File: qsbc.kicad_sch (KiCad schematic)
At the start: 0 parts

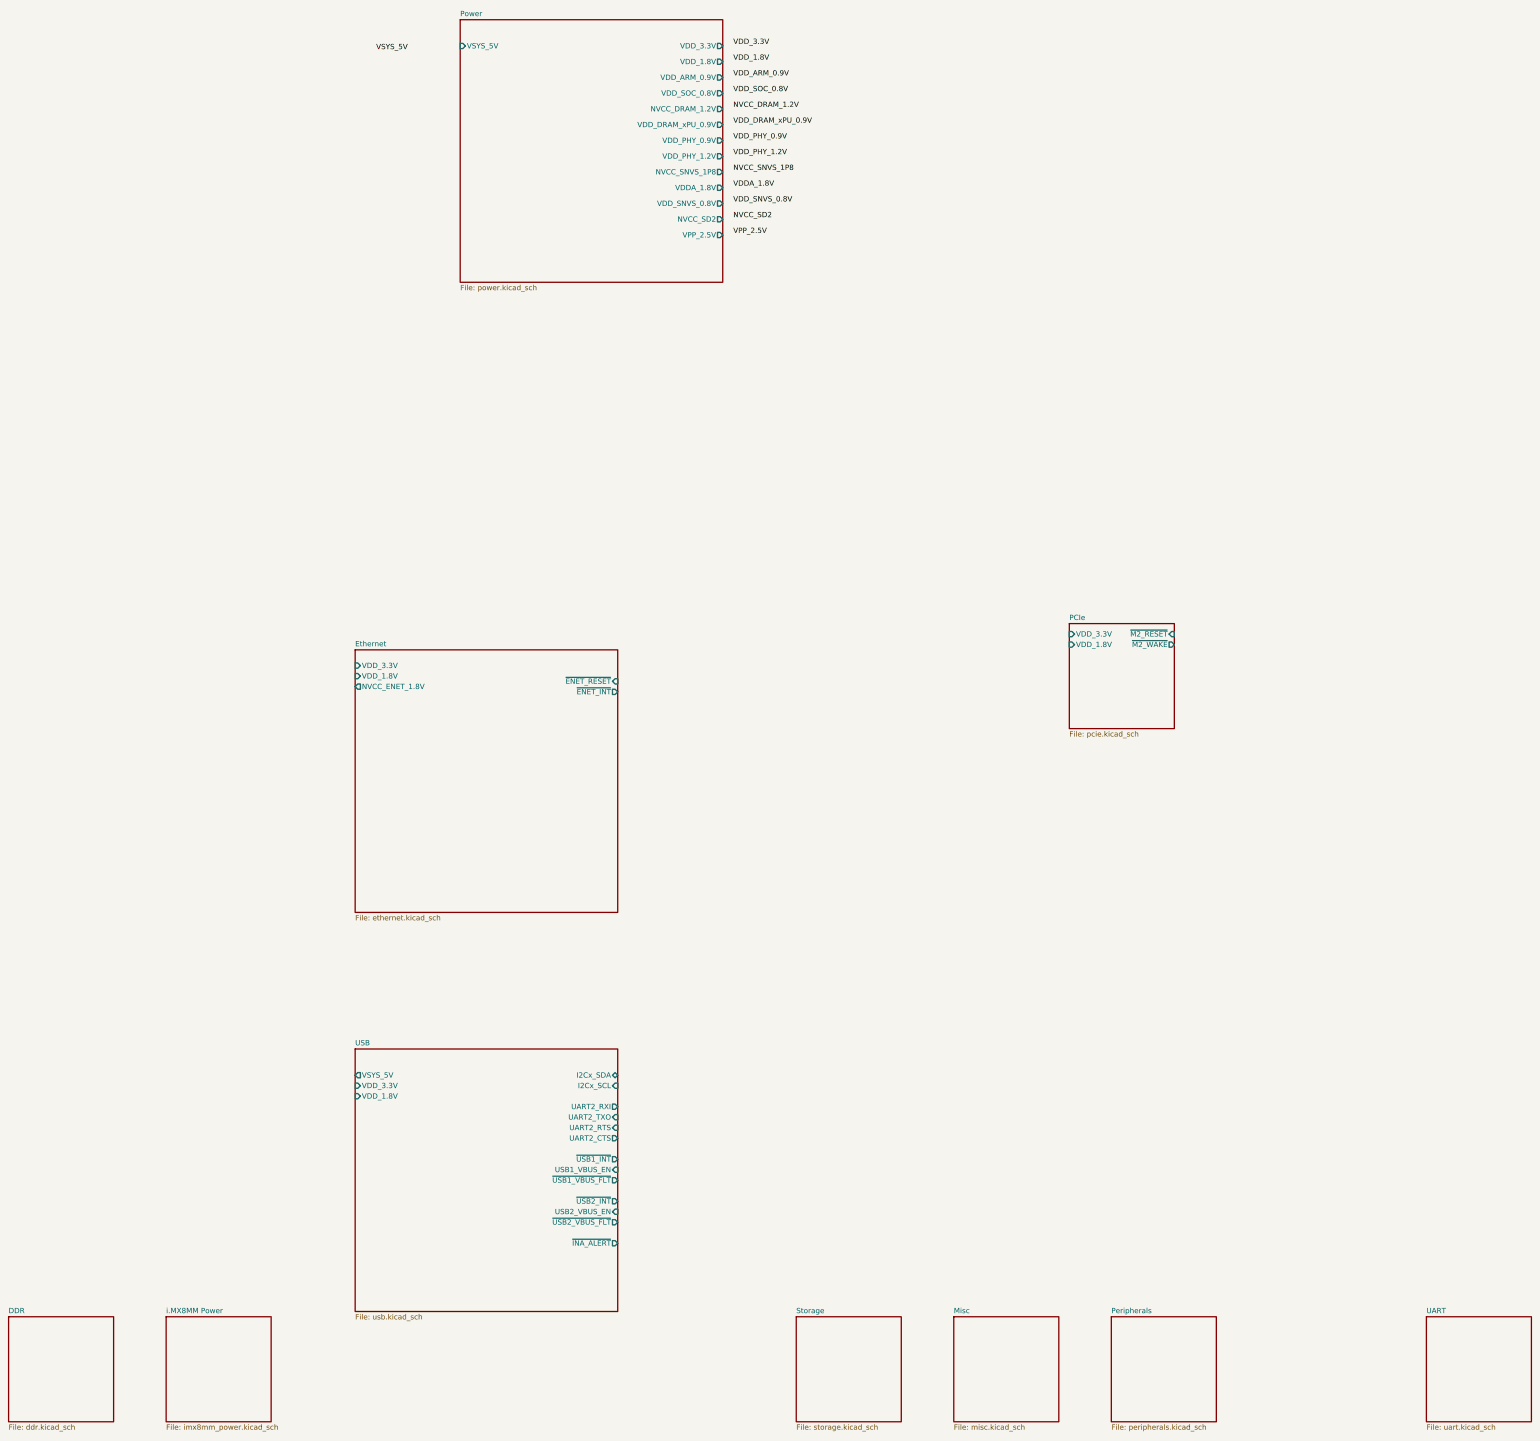
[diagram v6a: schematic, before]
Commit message: storage done, peri work, misc fixes
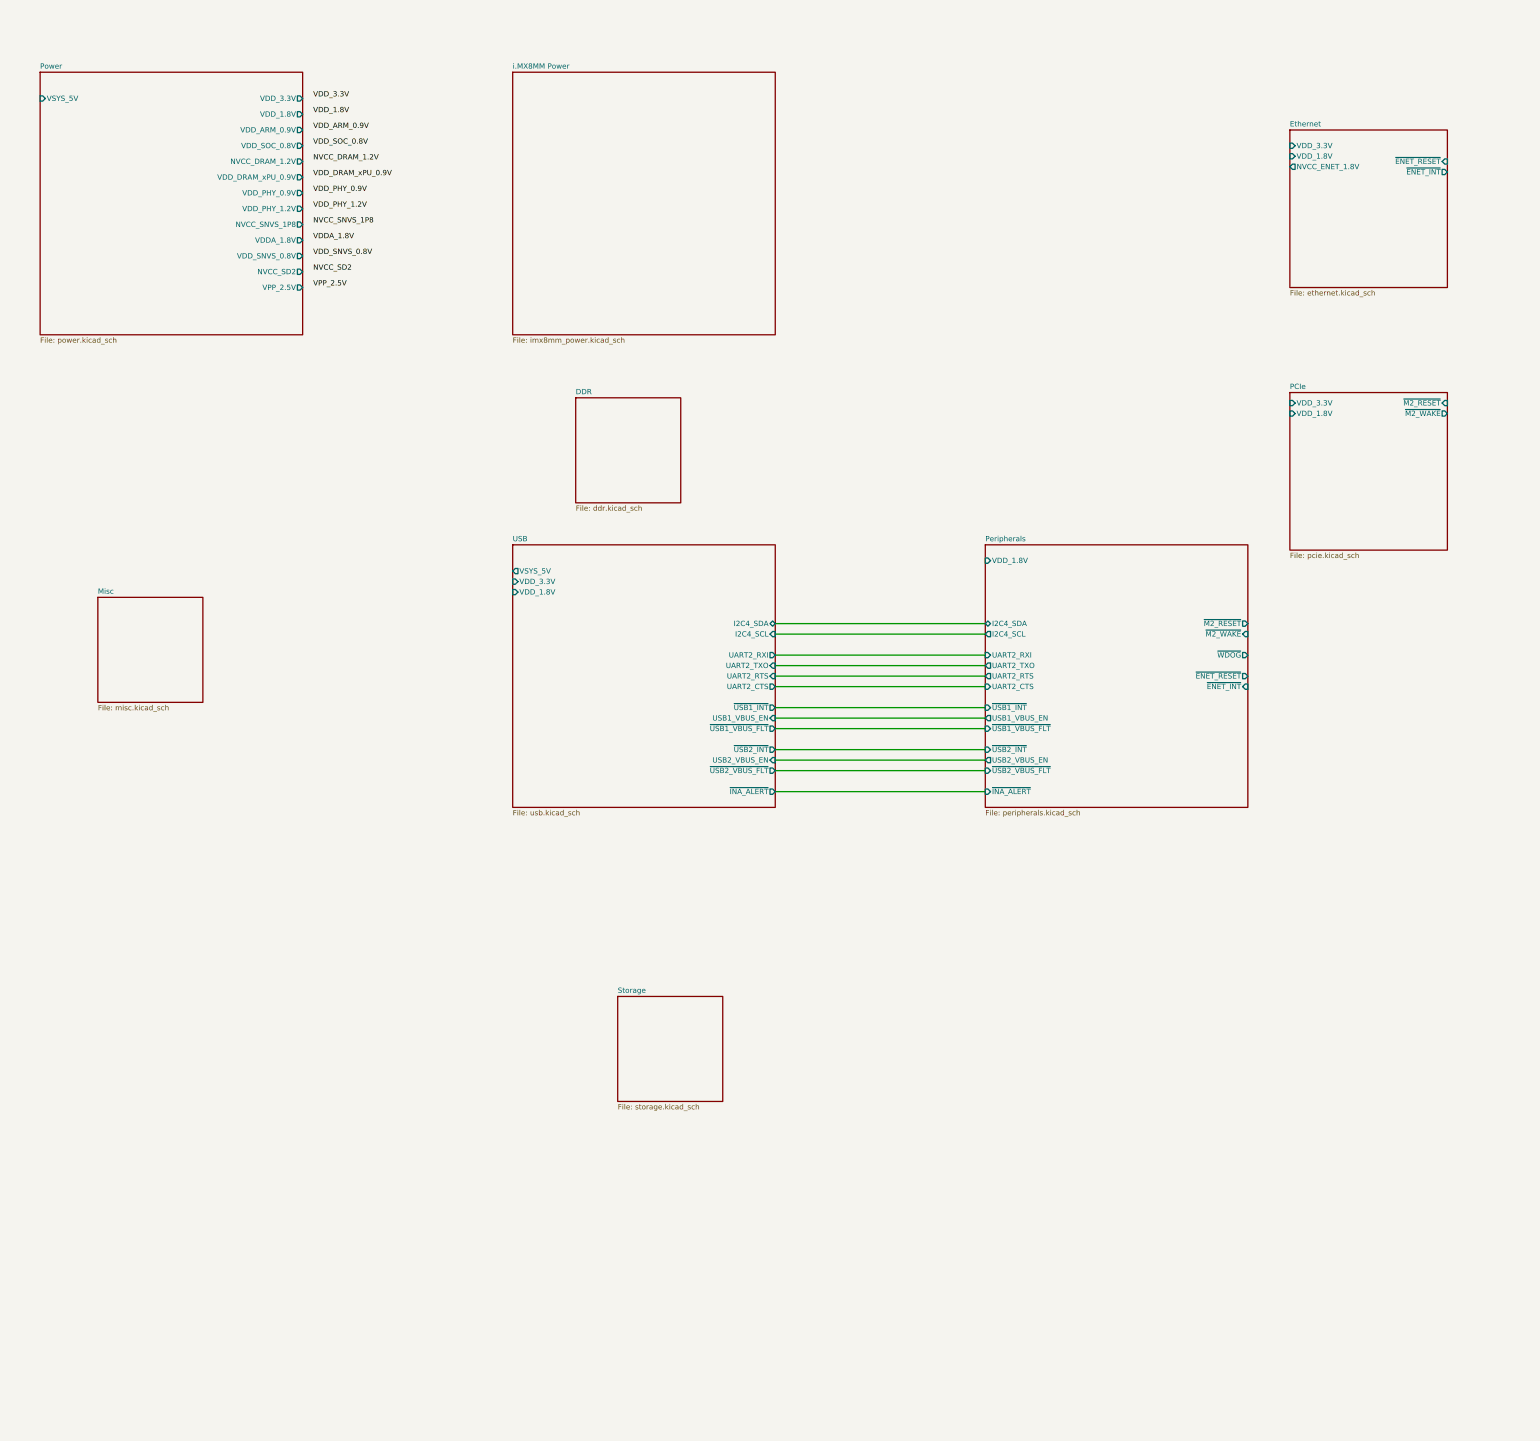
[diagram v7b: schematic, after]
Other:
- removed sheet UART
- sheet Peripherals ports: added I2C4_SCL, I2C4_SDA, UART2_CTS, UART2_RTS, UART2_RXI, UART2_TXO, USB1_VBUS_EN, USB2_VBUS_EN, VDD_1.8V, ~{ENET_INT}, ~{ENET_RESET}, ~{INA_ALERT}, ~{M2_RESET}, ~{M2_WAKE}, ~{USB1_INT}, ~{USB1_VBUS_FLT}, ~{USB2_INT}, ~{USB2_VBUS_FLT}, ~{WDOG}; removed none
- sheet USB ports: added I2C4_SCL, I2C4_SDA; removed I2Cx_SCL, I2Cx_SDA

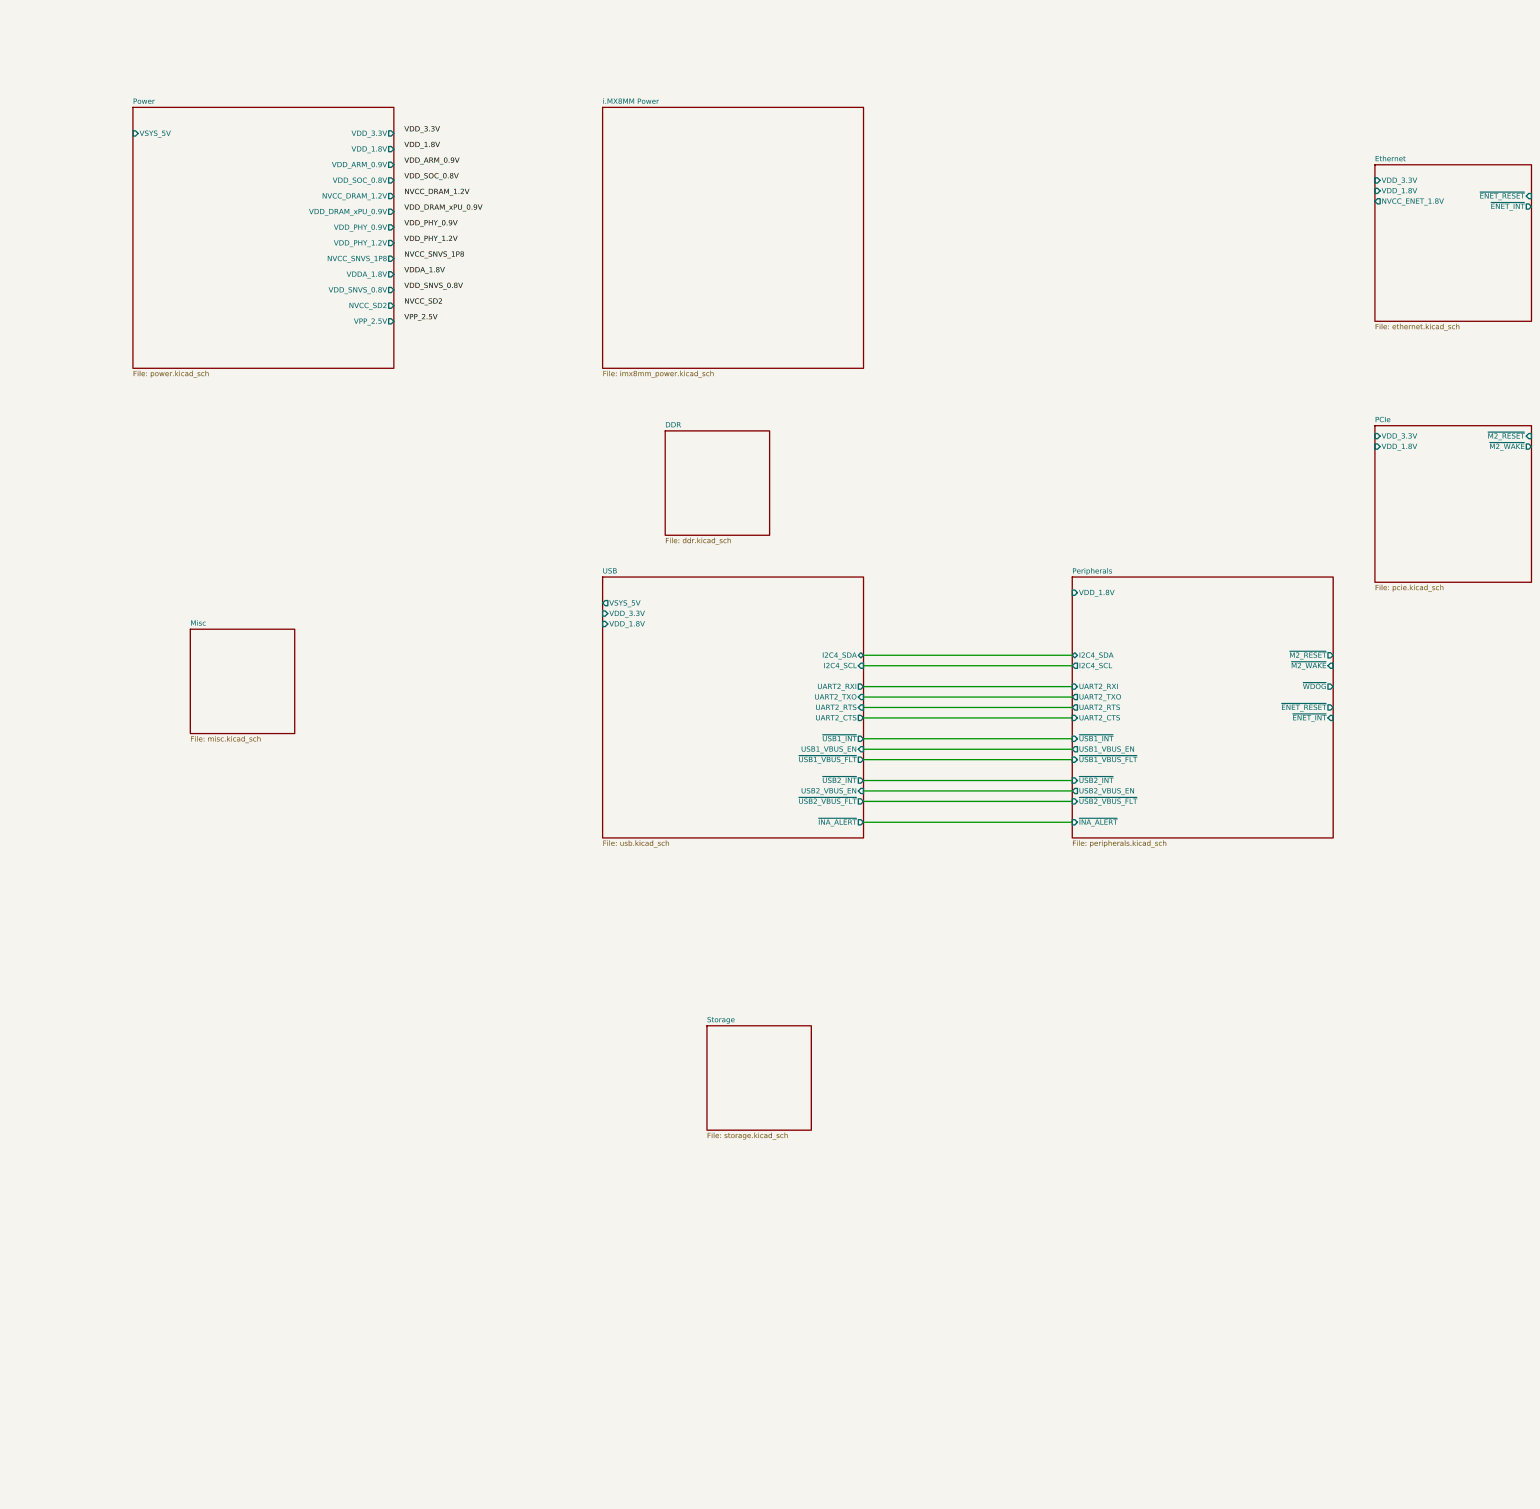
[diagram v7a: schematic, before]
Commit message: ddr: add dual die support, misc work
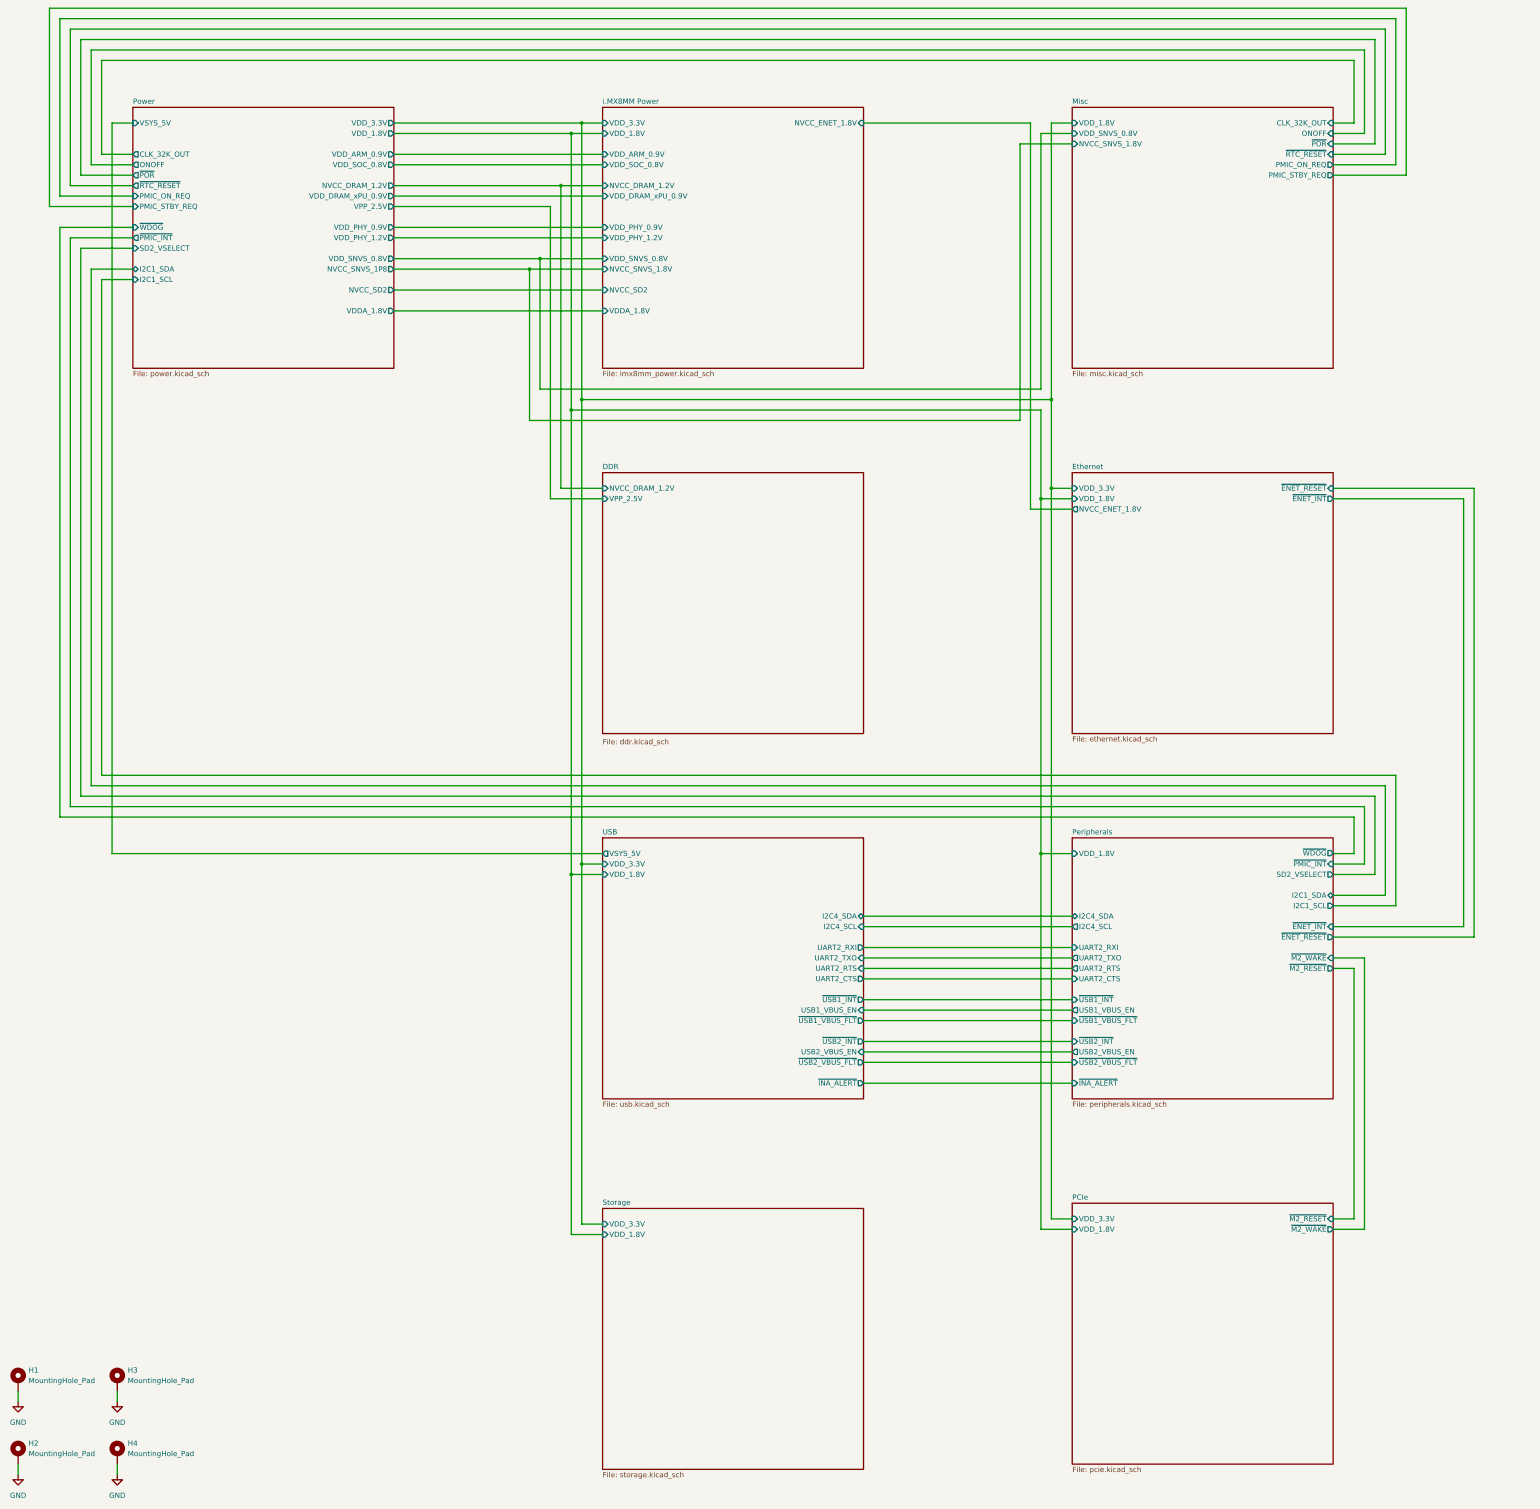
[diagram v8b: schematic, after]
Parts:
- added H1, H2, H3, H4: MountingHole_Pad, MountingHole:MountingHole_3.2mm_M3_Pad_Via, symbol Mechanical:MountingHole_Pad
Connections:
- new net GND: H1.1, H2.1, H3.1, H4.1
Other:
- sheet DDR ports: added NVCC_DRAM_1.2V, VPP_2.5V; removed none
- sheet Misc ports: added CLK_32K_OUT, NVCC_SNVS_1.8V, ONOFF, PMIC_ON_REQ, PMIC_STBY_REQ, VDD_1.8V, VDD_SNVS_0.8V, ~{POR}, ~{RTC_RESET}; removed none
- sheet Peripherals ports: added I2C1_SCL, I2C1_SDA, SD2_VSELECT, ~{PMIC_INT}; removed none
- sheet Power ports: added CLK_32K_OUT, I2C1_SCL, I2C1_SDA, ONOFF, PMIC_ON_REQ, PMIC_STBY_REQ, SD2_VSELECT, ~{PMIC_INT}, ~{POR}, ~{RTC_RESET}, ~{WDOG}; removed none
- sheet Storage ports: added VDD_1.8V, VDD_3.3V; removed none
- sheet i.MX8MM Power ports: added NVCC_DRAM_1.2V, NVCC_ENET_1.8V, NVCC_SD2, NVCC_SNVS_1.8V, VDDA_1.8V, VDD_1.8V, VDD_3.3V, VDD_ARM_0.9V, VDD_DRAM_xPU_0.9V, VDD_PHY_0.9V, VDD_PHY_1.2V, VDD_SNVS_0.8V, VDD_SOC_0.8V; removed none
- company: (none) -> Q-LAB
- title: (none) -> QSBC
